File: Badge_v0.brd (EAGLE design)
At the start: 73.6 x 58.1 mm, 67 parts, among them J3 CONN_82.54_SCREW, Q6 DMG3404, U1 MCP3421A3, U2 ATMEGA328P_TQFP, U23 FT231X-Q, U3 MCP15012.5V, U31 BME680, U4 ISL29125, U5 TPS7A0533DBV

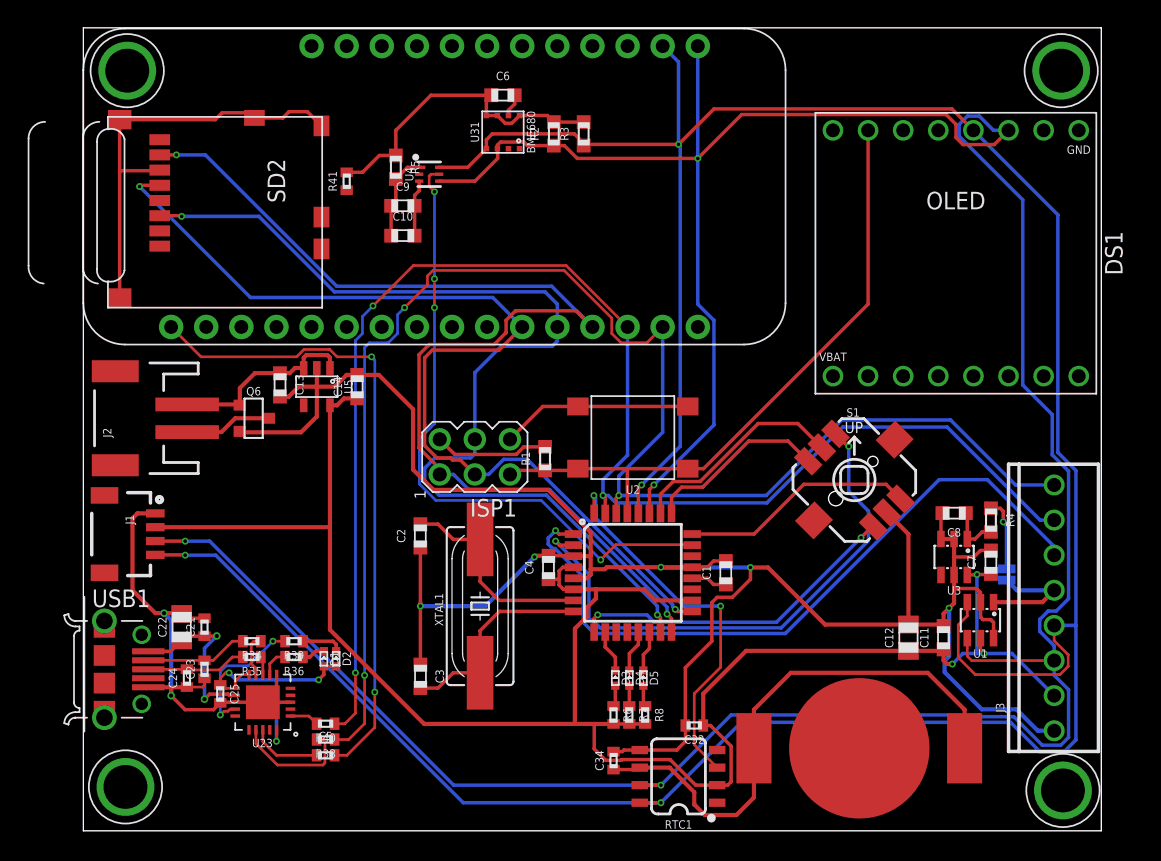
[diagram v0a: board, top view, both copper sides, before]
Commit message: Continued routing, functional
Layout is functional but cleanup, details (silkscreen, part numbers, etc) and review still required
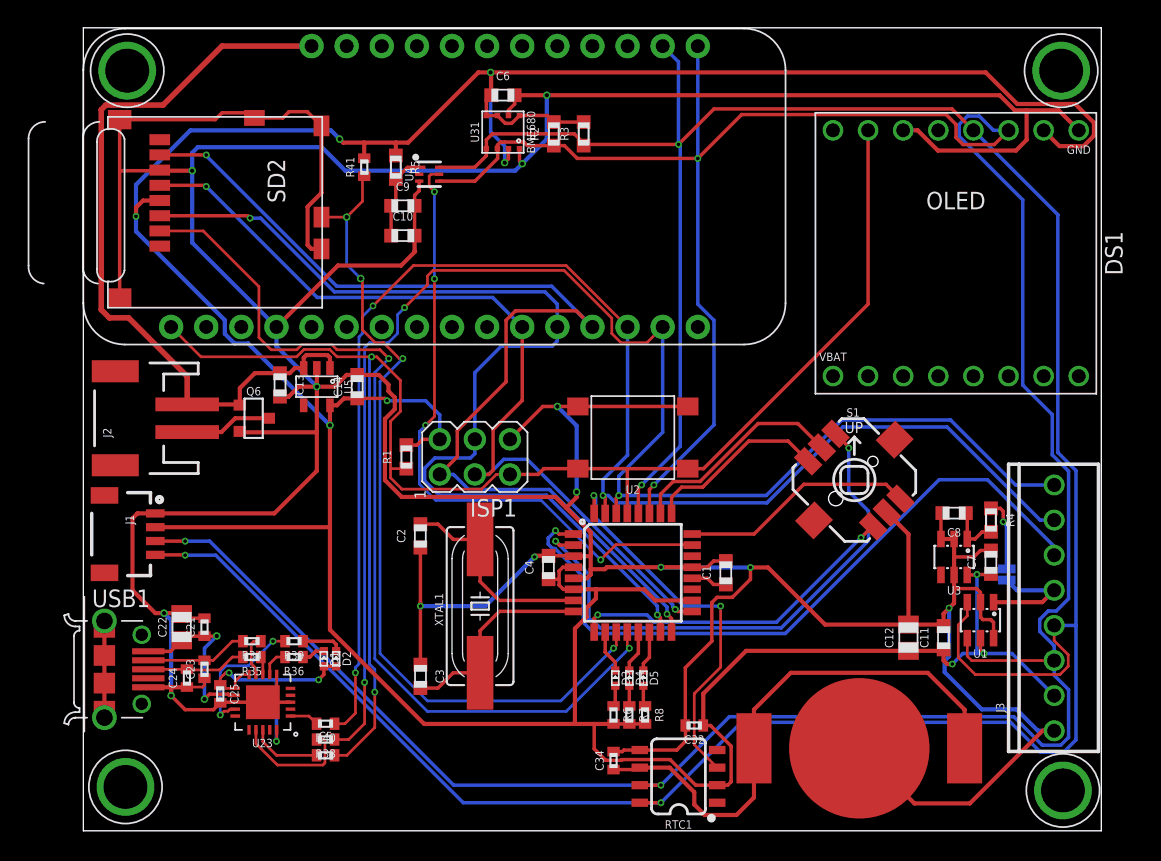
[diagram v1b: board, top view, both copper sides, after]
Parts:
- moved R1 10.0 mm to (23.4, 27.1)
- moved R41 1.63 mm to (20.3, 48.0)
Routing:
- net GND: track 248.9 -> 426.0 mm, vias 7 -> 13
- net 3V3: track 169.9 -> 277.0 mm, vias 3 -> 9
- net SD_CS: track 0.00 -> 68.1 mm, vias 0 -> 2
- net SD_CD: track 0.00 -> 60.9 mm, vias 0 -> 4
- net VIN+: track 13.8 -> 55.7 mm
- net RESET: track 93.3 -> 114.3 mm
- net SCK: track 73.0 -> 64.0 mm
- net N$1: track 0.00 -> 7.00 mm
- net MISO: track 83.0 -> 79.0 mm
